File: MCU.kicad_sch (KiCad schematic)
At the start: 26 parts

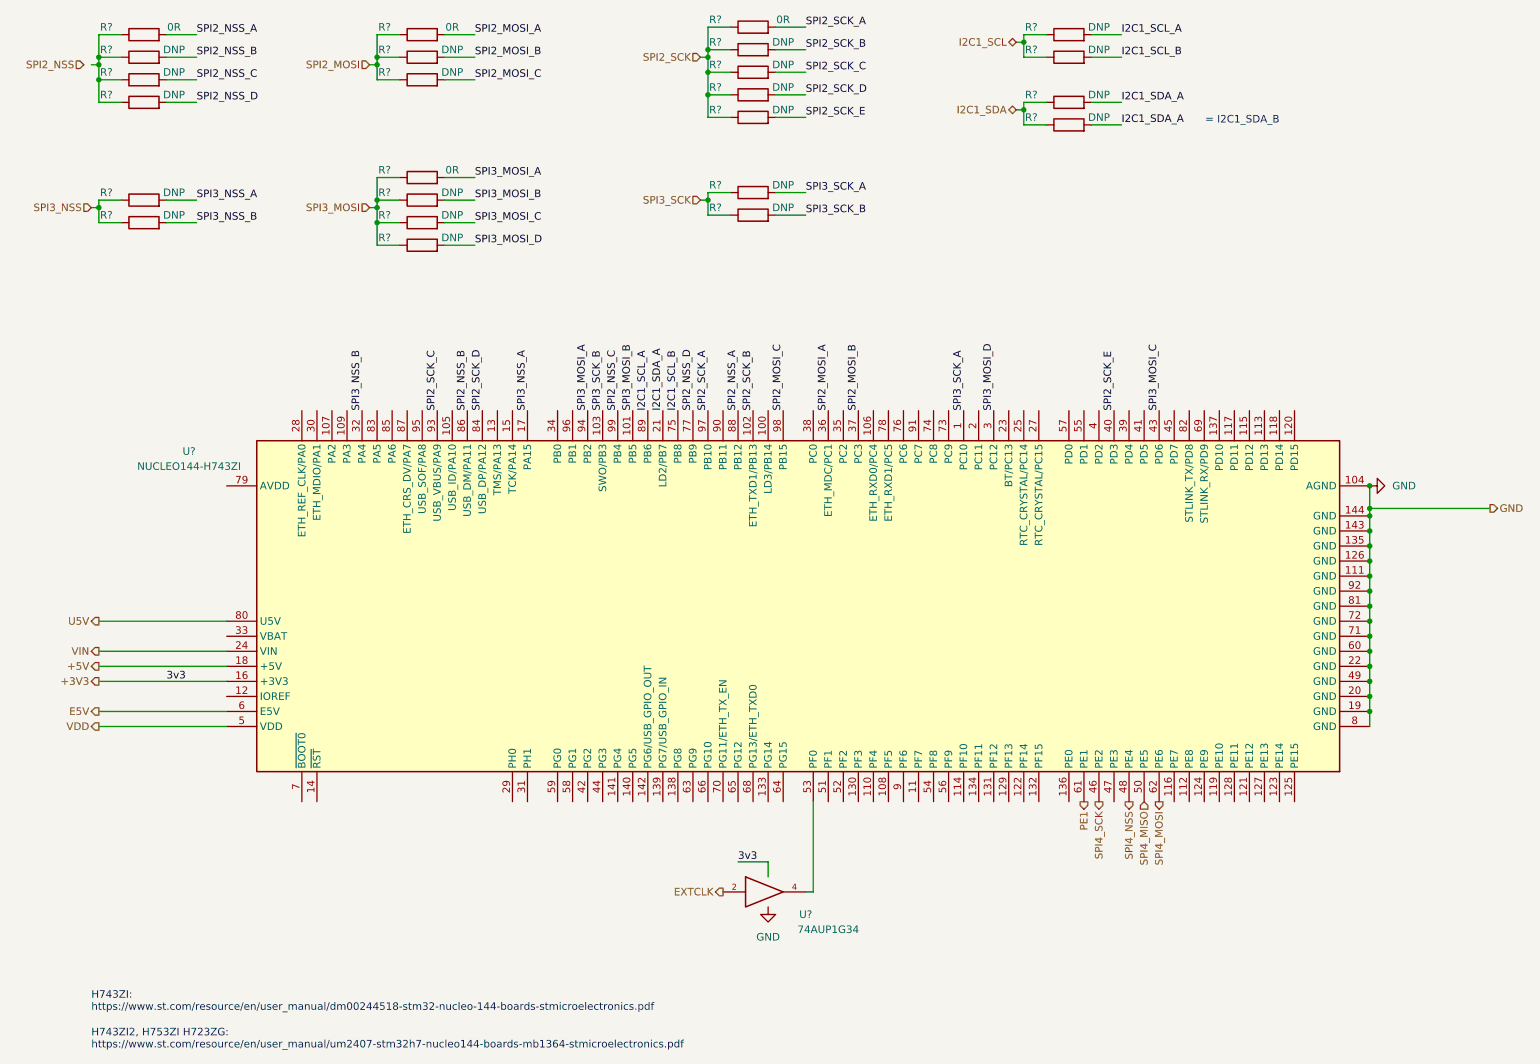
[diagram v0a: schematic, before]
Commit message: annotated and packages defined
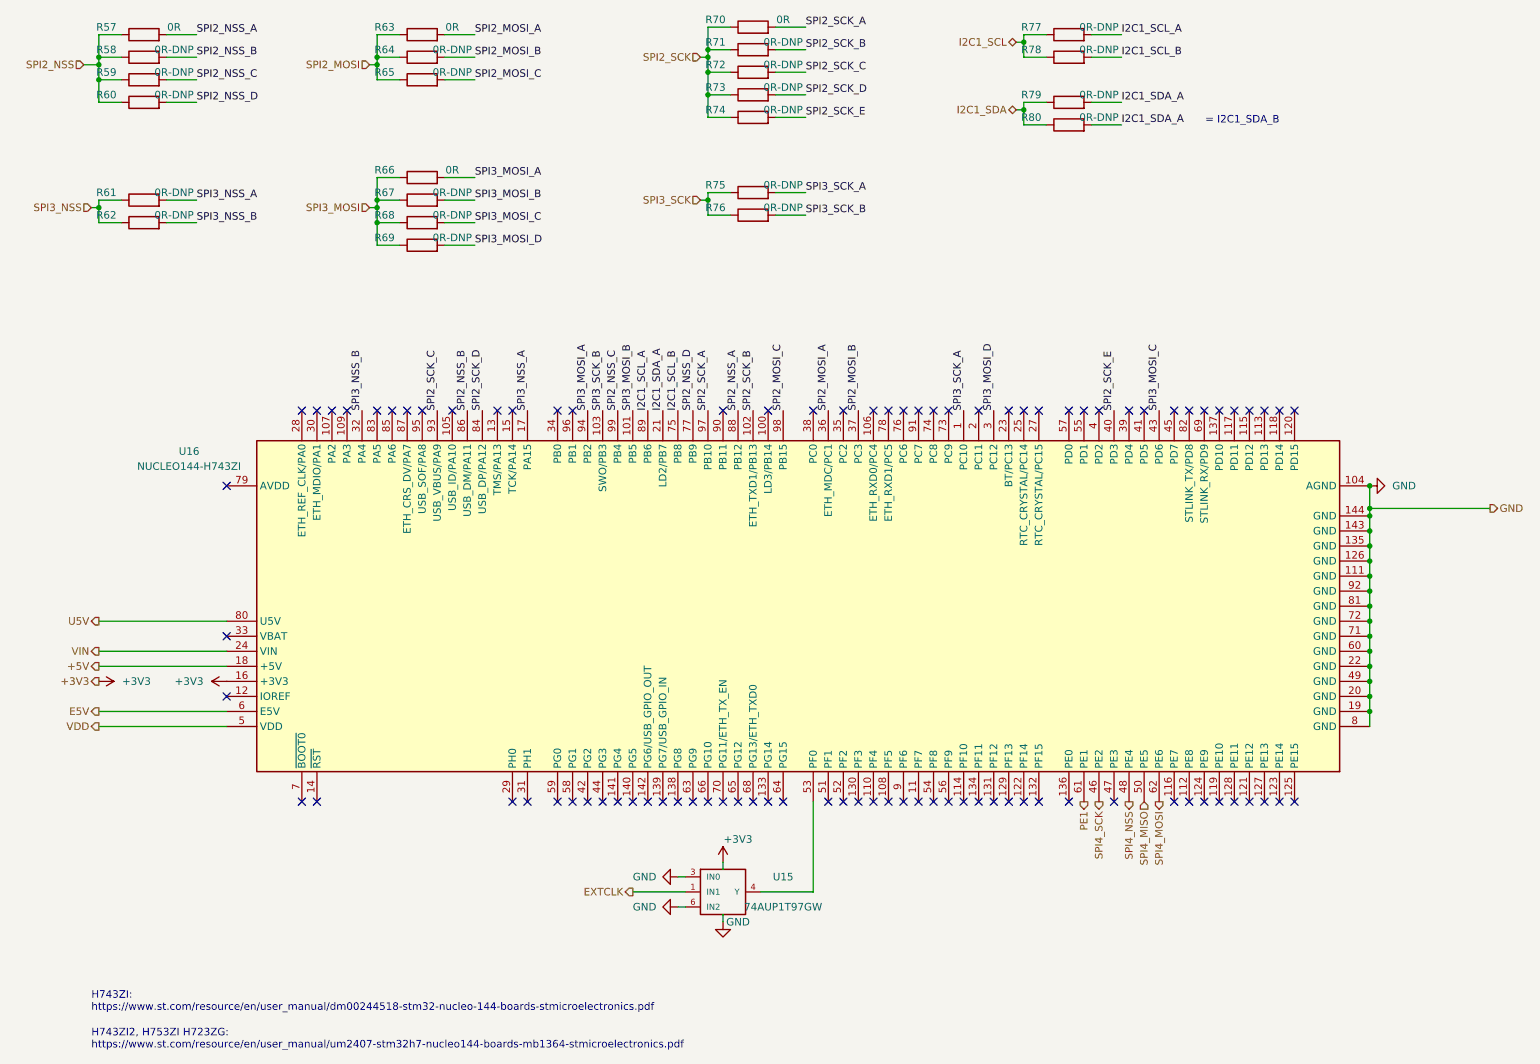
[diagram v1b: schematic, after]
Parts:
- removed U?: 74AUP1G34, symbol 74xGxx:74AUP1G34
- added U15: 74AUP1T97GW, Package_TO_SOT_SMD:SOT-363_SC-70-6_Handsoldering, symbol 74xGxx:74AUP1G97
- R57, R63, R66, R70: renamed from R?; footprint (none) -> Resistor_SMD:R_0805_2012Metric
- R58, R59, R60, R61, R62, R64, R65, R67, R68, R69, R71, R72, R73, R74, R75, R76, R77, R78, R79, R80: renamed from R?; value DNP -> 0R-DNP; footprint (none) -> Resistor_SMD:R_0805_2012Metric
- gave numbers to parts that had none: 1
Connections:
- net EXTCLK: now also U15.1 (IN1)
- net GND: now also U15.2 (GND), U15.3 (IN0), U15.6 (IN2)
- net SPI2_NSS: now also R57.1, R58.1, R59.1, R60.1
- net at U16.53 (PF0): now also U15.4 (Y)
- net VCC renamed +3V3
- net +3V3: now also U15.5 (VCC)
- no-connect marks 0 -> 90
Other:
- company: (none) -> papamidas DM1CR
- title: (none) -> H7DDCADC

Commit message: placement_in_progress 1
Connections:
- net PF0_50: now reaches U15.4 (Y), U16.53 (PF0)
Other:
- note added: "NXP Suffix GW = TSSOP6 (SOT363-2, 0.65 mm pitch)"
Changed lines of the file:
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@@
     (effects (font (size 1.27 1.27)) (justify right bottom))
+  )
+  (text "NXP Suffix GW = TSSOP6 (SOT363-2, 0.65 mm pitch)" (at 110.49 176.53 0)
+    (effects (font (size 1.27 1.27)) (justify left bottom))
   )
   (text "H743ZI2, H753ZI H723ZG:\nhttps://www.st.com/resource/en/user_manual/um2407-stm32h7-nucleo144-boards-mb1364-stmicroelectronics.pdf"
@@
     (effects (font (size 1.27 1.27)) (justify left bottom))
   )
+  (label "PF0_50" (at 152.4 157.48 0)
+    (effects (font (size 1.27 1.27)) (justify left bottom))
+  )

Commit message: placement 80 percent
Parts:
- R57, R58, R59, R60, R61, R62, R63, R64, R65, R66, R67, R68, R69, R70, R71, R72, R73, R74, R75, R76, R77, R78, R79, R80: footprint Resistor_SMD:R_0805_2012Metric -> Resistor_SMD:R_0402_1005Metric_Pad0.72x0.64mm_HandSolder
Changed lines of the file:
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@@
     (property "Reference" "R61" (id 0) (at 33.02 45.72 90))
     (property "Value" "0R-DNP" (id 1) (at 44.45 45.72 90))
-    (property "Footprint" "Resistor_SMD:R_0805_2012Metric" (id 2) (at 39.37 48.768 90)
+    (property "Footprint" "Resistor_SMD:R_0402_1005Metric_Pad0.72x0.64mm_HandSolder" (id 2) (at 39.37 48.768 90)
       (effects (font (size 1.27 1.27)) hide)
     )
@@
     (property "Reference" "R64" (id 0) (at 80.01 21.59 90))
     (property "Value" "0R-DNP" (id 1) (at 91.44 21.59 90))
-    (property "Footprint" "Resistor_SMD:R_0805_2012Metric" (id 2) (at 86.36 24.638 90)
+    (property "Footprint" "Resistor_SMD:R_0402_1005Metric_Pad0.72x0.64mm_HandSolder" (id 2) (at 86.36 24.638 90)
       (effects (font (size 1.27 1.27)) hide)
     )
@@
     (property "Reference" "R57" (id 0) (at 33.02 17.78 90))
     (property "Value" "0R" (id 1) (at 44.45 17.78 90))
-    (property "Footprint" "Resistor_SMD:R_0805_2012Metric" (id 2) (at 39.37 20.828 90)
+    (property "Footprint" "Resistor_SMD:R_0402_1005Metric_Pad0.72x0.64mm_HandSolder" (id 2) (at 39.37 20.828 90)
       (effects (font (size 1.27 1.27)) hide)
     )
@@
     (property "Reference" "R68" (id 0) (at 80.01 49.53 90))
     (property "Value" "0R-DNP" (id 1) (at 91.44 49.53 90))
-    (property "Footprint" "Resistor_SMD:R_0805_2012Metric" (id 2) (at 86.36 52.578 90)
+    (property "Footprint" "Resistor_SMD:R_0402_1005Metric_Pad0.72x0.64mm_HandSolder" (id 2) (at 86.36 52.578 90)
       (effects (font (size 1.27 1.27)) hide)
     )
@@
     (property "Reference" "R69" (id 0) (at 80.01 53.34 90))
     (property "Value" "0R-DNP" (id 1) (at 91.44 53.34 90))
-    (property "Footprint" "Resistor_SMD:R_0805_2012Metric" (id 2) (at 86.36 56.388 90)
+    (property "Footprint" "Resistor_SMD:R_0402_1005Metric_Pad0.72x0.64mm_HandSolder" (id 2) (at 86.36 56.388 90)
       (effects (font (size 1.27 1.27)) hide)
     )
@@
     (property "Reference" "R59" (id 0) (at 33.02 25.4 90))
     (property "Value" "0R-DNP" (id 1) (at 44.45 25.4 90))
-    (property "Footprint" "Resistor_SMD:R_0805_2012Metric" (id 2) (at 39.37 28.448 90)
+    (property "Footprint" "Resistor_SMD:R_0402_1005Metric_Pad0.72x0.64mm_HandSolder" (id 2) (at 39.37 28.448 90)
       (effects (font (size 1.27 1.27)) hide)
     )
@@
     (property "Reference" "R78" (id 0) (at 189.23 21.59 90))
     (property "Value" "0R-DNP" (id 1) (at 200.66 21.59 90))
-    (property "Footprint" "Resistor_SMD:R_0805_2012Metric" (id 2) (at 195.58 24.638 90)
+    (property "Footprint" "Resistor_SMD:R_0402_1005Metric_Pad0.72x0.64mm_HandSolder" (id 2) (at 195.58 24.638 90)
       (effects (font (size 1.27 1.27)) hide)
     )
@@
     (property "Reference" "R63" (id 0) (at 80.01 17.78 90))
     (property "Value" "0R" (id 1) (at 91.44 17.78 90))
-    (property "Footprint" "Resistor_SMD:R_0805_2012Metric" (id 2) (at 86.36 20.828 90)
+    (property "Footprint" "Resistor_SMD:R_0402_1005Metric_Pad0.72x0.64mm_HandSolder" (id 2) (at 86.36 20.828 90)
       (effects (font (size 1.27 1.27)) hide)
     )
@@
     (property "Reference" "R75" (id 0) (at 135.89 44.45 90))
     (property "Value" "0R-DNP" (id 1) (at 147.32 44.45 90))
-    (property "Footprint" "Resistor_SMD:R_0805_2012Metric" (id 2) (at 142.24 47.498 90)
+    (property "Footprint" "Resistor_SMD:R_0402_1005Metric_Pad0.72x0.64mm_HandSolder" (id 2) (at 142.24 47.498 90)
       (effects (font (size 1.27 1.27)) hide)
     )
@@
     (property "Reference" "R80" (id 0) (at 189.23 33.02 90))
     (property "Value" "0R-DNP" (id 1) (at 200.66 33.02 90))
-    (property "Footprint" "Resistor_SMD:R_0805_2012Metric" (id 2) (at 195.58 36.068 90)
+    (property "Footprint" "Resistor_SMD:R_0402_1005Metric_Pad0.72x0.64mm_HandSolder" (id 2) (at 195.58 36.068 90)
       (effects (font (size 1.27 1.27)) hide)
     )
@@
     (property "Reference" "R79" (id 0) (at 189.23 29.21 90))
     (property "Value" "0R-DNP" (id 1) (at 200.66 29.21 90))
-    (property "Footprint" "Resistor_SMD:R_0805_2012Metric" (id 2) (at 195.58 32.258 90)
+    (property "Footprint" "Resistor_SMD:R_0402_1005Metric_Pad0.72x0.64mm_HandSolder" (id 2) (at 195.58 32.258 90)
       (effects (font (size 1.27 1.27)) hide)
     )
@@
     (property "Reference" "R70" (id 0) (at 135.89 16.51 90))
     (property "Value" "0R" (id 1) (at 147.32 16.51 90))
-    (property "Footprint" "Resistor_SMD:R_0805_2012Metric" (id 2) (at 142.24 19.558 90)
+    (property "Footprint" "Resistor_SMD:R_0402_1005Metric_Pad0.72x0.64mm_HandSolder" (id 2) (at 142.24 19.558 90)
       (effects (font (size 1.27 1.27)) hide)
     )
@@
     (property "Reference" "R76" (id 0) (at 135.89 48.26 90))
     (property "Value" "0R-DNP" (id 1) (at 147.32 48.26 90))
-    (property "Footprint" "Resistor_SMD:R_0805_2012Metric" (id 2) (at 142.24 51.308 90)
+    (property "Footprint" "Resistor_SMD:R_0402_1005Metric_Pad0.72x0.64mm_HandSolder" (id 2) (at 142.24 51.308 90)
       (effects (font (size 1.27 1.27)) hide)
     )
@@
     (property "Reference" "R62" (id 0) (at 33.02 49.53 90))
     (property "Value" "0R-DNP" (id 1) (at 44.45 49.53 90))
-    (property "Footprint" "Resistor_SMD:R_0805_2012Metric" (id 2) (at 39.37 52.578 90)
+    (property "Footprint" "Resistor_SMD:R_0402_1005Metric_Pad0.72x0.64mm_HandSolder" (id 2) (at 39.37 52.578 90)
       (effects (font (size 1.27 1.27)) hide)
     )
@@
     (property "Reference" "R65" (id 0) (at 80.01 25.4 90))
     (property "Value" "0R-DNP" (id 1) (at 91.44 25.4 90))
-    (property "Footprint" "Resistor_SMD:R_0805_2012Metric" (id 2) (at 86.36 28.448 90)
+    (property "Footprint" "Resistor_SMD:R_0402_1005Metric_Pad0.72x0.64mm_HandSolder" (id 2) (at 86.36 28.448 90)
       (effects (font (size 1.27 1.27)) hide)
     )
@@
     (property "Reference" "R58" (id 0) (at 33.02 21.59 90))
     (property "Value" "0R-DNP" (id 1) (at 44.45 21.59 90))
-    (property "Footprint" "Resistor_SMD:R_0805_2012Metric" (id 2) (at 39.37 24.638 90)
+    (property "Footprint" "Resistor_SMD:R_0402_1005Metric_Pad0.72x0.64mm_HandSolder" (id 2) (at 39.37 24.638 90)
       (effects (font (size 1.27 1.27)) hide)
     )
@@
     (property "Reference" "R66" (id 0) (at 80.01 41.91 90))
     (property "Value" "0R" (id 1) (at 91.44 41.91 90))
-    (property "Footprint" "Resistor_SMD:R_0805_2012Metric" (id 2) (at 86.36 44.958 90)
+    (property "Footprint" "Resistor_SMD:R_0402_1005Metric_Pad0.72x0.64mm_HandSolder" (id 2) (at 86.36 44.958 90)
       (effects (font (size 1.27 1.27)) hide)
     )
@@
     (property "Reference" "R71" (id 0) (at 135.89 20.32 90))
     (property "Value" "0R-DNP" (id 1) (at 147.32 20.32 90))
-    (property "Footprint" "Resistor_SMD:R_0805_2012Metric" (id 2) (at 142.24 23.368 90)
+    (property "Footprint" "Resistor_SMD:R_0402_1005Metric_Pad0.72x0.64mm_HandSolder" (id 2) (at 142.24 23.368 90)
       (effects (font (size 1.27 1.27)) hide)
     )
@@
     (property "Reference" "R67" (id 0) (at 80.01 45.72 90))
     (property "Value" "0R-DNP" (id 1) (at 91.44 45.72 90))
-    (property "Footprint" "Resistor_SMD:R_0805_2012Metric" (id 2) (at 86.36 48.768 90)
+    (property "Footprint" "Resistor_SMD:R_0402_1005Metric_Pad0.72x0.64mm_HandSolder" (id 2) (at 86.36 48.768 90)
       (effects (font (size 1.27 1.27)) hide)
     )
@@
     (property "Reference" "R60" (id 0) (at 33.02 29.21 90))
     (property "Value" "0R-DNP" (id 1) (at 44.45 29.21 90))
-    (property "Footprint" "Resistor_SMD:R_0805_2012Metric" (id 2) (at 39.37 32.258 90)
+    (property "Footprint" "Resistor_SMD:R_0402_1005Metric_Pad0.72x0.64mm_HandSolder" (id 2) (at 39.37 32.258 90)
       (effects (font (size 1.27 1.27)) hide)
     )
@@
     (property "Reference" "R73" (id 0) (at 135.89 27.94 90))
     (property "Value" "0R-DNP" (id 1) (at 147.32 27.94 90))
-    (property "Footprint" "Resistor_SMD:R_0805_2012Metric" (id 2) (at 142.24 30.988 90)
+    (property "Footprint" "Resistor_SMD:R_0402_1005Metric_Pad0.72x0.64mm_HandSolder" (id 2) (at 142.24 30.988 90)
       (effects (font (size 1.27 1.27)) hide)
     )
@@
     (property "Reference" "R74" (id 0) (at 135.89 31.75 90))
     (property "Value" "0R-DNP" (id 1) (at 147.32 31.75 90))
-    (property "Footprint" "Resistor_SMD:R_0805_2012Metric" (id 2) (at 142.24 34.798 90)
+    (property "Footprint" "Resistor_SMD:R_0402_1005Metric_Pad0.72x0.64mm_HandSolder" (id 2) (at 142.24 34.798 90)
       (effects (font (size 1.27 1.27)) hide)
     )
@@
     (property "Reference" "R77" (id 0) (at 189.23 17.78 90))
     (property "Value" "0R-DNP" (id 1) (at 200.66 17.78 90))
-    (property "Footprint" "Resistor_SMD:R_0805_2012Metric" (id 2) (at 195.58 20.828 90)
+    (property "Footprint" "Resistor_SMD:R_0402_1005Metric_Pad0.72x0.64mm_HandSolder" (id 2) (at 195.58 20.828 90)
       (effects (font (size 1.27 1.27)) hide)
     )
@@
     (property "Reference" "R72" (id 0) (at 135.89 24.13 90))
     (property "Value" "0R-DNP" (id 1) (at 147.32 24.13 90))
-    (property "Footprint" "Resistor_SMD:R_0805_2012Metric" (id 2) (at 142.24 27.178 90)
-      (effects (font (size 1.27 1.27)) hide)
-    )
+    (property "Footprint" "Resistor_SMD:R_0402_1005Metric_Pad0.72x0.64mm_HandSolder" (id 2) (at 142.24 27.178 90)
+      (effects (font (size 1.27 1.27)) hide)
+    )

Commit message: routing in progress 1
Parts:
- removed U16: NUCLEO144-H743ZI, Module:ST_Morpho_Connector_144_STLink, symbol MCU_Module:NUCLEO144-H743ZI
- added C38: 100nF, Capacitor_SMD:C_0805_2012Metric, symbol Device:C_Small
- added FB5: Ferrite_0805, Resistor_SMD:R_0805_2012Metric, symbol Device:FerriteBead_Small
- added U16: NUCLEO144-H743ZI_DM1CR, Module:ST_Morpho_Connector_144_STLink, symbol DM1CR_Library_loc:NUCLEO144-H743ZI_DM1CR
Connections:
- net +3V3: now also U16.16 (+3V3); no longer U15.5 (VCC)
- net +5V: now also U16.18 (+5V)
- net E5V: now also U16.6 (E5V)
- net GND: now also C38.2, U16.104 (AGND), U16.111 (GND), U16.126 (GND), U16.135 (GND), U16.143 (GND), U16.144 (GND), U16.19 (GND), U16.20 (GND), U16.22 (GND), U16.49 (GND), U16.60 (GND), U16.71 (GND), U16.72 (GND), U16.8 (GND), U16.81 (GND), U16.92 (GND)
- net I2C1_SCL_A: now also U16.89 (PB6)
- net I2C1_SCL_B: now also U16.75 (PB8)
- net I2C1_SDA_A: now also U16.21 (LD2/PB7); no longer R80.2
- net PE1: now also U16.61 (PE1)
- net PF0_50: now also U16.53 (PF0)
- net SPI2_MOSI_A: now also U16.36 (ETH_MDC/PC1)
- net SPI2_MOSI_B: now also U16.37 (PC3)
- net SPI2_MOSI_C: now also U16.98 (PB15)
- net SPI2_NSS_A: now also U16.88 (PB12)
- net SPI2_NSS_B: now also U16.86 (USB_DM/PA11)
- net SPI2_NSS_C: now also U16.99 (PB4)
- net SPI2_NSS_D: now also R80.2, U16.77 (PB9)
- net SPI2_SCK_A: now also U16.97 (PB10)
- net SPI2_SCK_B: now also U16.102 (ETH_TXD1/PB13)
- net SPI2_SCK_C: now also U16.93 (USB_VBUS/PA9)
- net SPI2_SCK_D: now also U16.84 (USB_DP/PA12)
- net SPI2_SCK_E: now also U16.40 (PD3)
- net SPI3_MOSI_A: now also U16.94 (PB2)
- net SPI3_MOSI_B: now also U16.101 (PB5)
- net SPI3_MOSI_C: now also U16.43 (PD6)
- net SPI3_MOSI_D: now also U16.3 (PC12)
- net SPI3_NSS_A: now also U16.17 (PA15)
- net SPI3_NSS_B: now also U16.32 (PA4)
- net SPI3_SCK_A: now also U16.1 (PC10)
- net SPI3_SCK_B: now also U16.103 (SWO/PB3)
- net SPI4_MISO: now also U16.50 (PE5)
- net SPI4_MOSI: now also U16.62 (PE6)
- net SPI4_NSS: now also U16.48 (PE4)
- net SPI4_SCK: now also U16.46 (PE2)
- net U5V: now also U16.80 (U5V)
- net VDD: now also U16.5 (VDD)
- net VIN: now also U16.24 (VIN)
- new net VCC: C38.1, FB5.1, U15.5 (VCC)
- new net VCC_1T97: FB5.2
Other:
- note added: "= I2C1_SDA_B (PB7, PB9)"
- note removed: "= I2C1_SDA_B"

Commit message: routing done
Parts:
- U16: footprint Module:ST_Morpho_Connector_144_STLink -> H7DDCADC:ST_Morpho_Connector_144_STLink
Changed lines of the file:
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@@
     (property "Reference" "U16" (id 0) (at 43.18 89.4205 90))
     (property "Value" "NUCLEO144-H743ZI_DM1CR" (id 1) (at 43.18 91.9605 90))
-    (property "Footprint" "Module:ST_Morpho_Connector_144_STLink" (id 2) (at 242.57 93.98 0)
+    (property "Footprint" "H7DDCADC:ST_Morpho_Connector_144_STLink" (id 2) (at 242.57 93.98 0)
       (effects (font (size 1.27 1.27)) (justify left) hide)
     )
